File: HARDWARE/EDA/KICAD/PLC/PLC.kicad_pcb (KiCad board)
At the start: 2 copper layers, 200.5 x 200.5 mm, 0 parts

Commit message: Schematic finished
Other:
- outline, holes or cut-outs redrawn
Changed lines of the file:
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@@
   (general
     (thickness 1.6)
-    (drawings 11)
+    (drawings 19)
     (tracks 0)
     (zones 0)
@@
     (uvia_drill 0.1)
   )
+  (gr_circle (center 148 153) (end 146.5 153) (layer Edge.Cuts) (width 0.05))
+  (gr_circle (center 98 103) (end 96.5 103) (layer Edge.Cuts) (width 0.05))
+  (gr_circle (center 148 53) (end 146.5 53) (layer Edge.Cuts) (width 0.05))
+  (gr_circle (center 198 103) (end 196.5 103) (layer Edge.Cuts) (width 0.05))
+  (target plus (at 148 153) (size 5) (width 0.05) (layer Edge.Cuts))
+  (target plus (at 148 53) (size 5) (width 0.05) (layer Edge.Cuts))
+  (target plus (at 198 103) (size 5) (width 0.05) (layer Edge.Cuts))
+  (target plus (at 98 103) (size 5) (width 0.05) (layer Edge.Cuts))
   (gr_circle (center 148 103) (end 243 103) (layer B.SilkS) (width 0.12))
   (gr_circle (center 148 103) (end 243 103) (layer F.SilkS) (width 0.12))

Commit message: pause work
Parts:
- added C1: 250V, Capacitor_THT:CP_Radial_D10.0mm_P5.00mm, F.Cu at (271.8, -24.7)
- added D1: 1N4007, Diode_THT:D_DO-41_SOD81_P10.16mm_Horizontal, F.Cu at (243.7, -0.48)
- added D10: LED 3V, LED_THT:LED_D5.0mm_Clear, F.Cu at (659.8, -7.40)
- added D100: LED 3V, LED_THT:LED_D5.0mm_Clear, F.Cu at (407.5, 15.0)
- added D101: LED 3V, LED_THT:LED_D5.0mm_Clear, F.Cu at (400.0, 22.6)
- added D102: LED 3V, LED_THT:LED_D5.0mm_Clear, F.Cu at (392.5, 30.1)
- added D103: LED 3V, LED_THT:LED_D5.0mm_Clear, F.Cu at (385.0, 37.6)
- added D104: LED 3V, LED_THT:LED_D5.0mm_Clear, F.Cu at (370.0, 52.8)
- added D105: LED 3V, LED_THT:LED_D5.0mm_Clear, F.Cu at (362.5, 60.3)
- added D106: LED 3V, LED_THT:LED_D5.0mm_Clear, F.Cu at (355.0, 67.8)
- added D107: LED 3V, LED_THT:LED_D5.0mm_Clear, F.Cu at (347.5, 75.4)
- added D108: LED 3V, LED_THT:LED_D5.0mm_Clear, F.Cu at (340.0, 83.0)
- added D109: LED 3V, LED_THT:LED_D5.0mm_Clear, F.Cu at (377.5, 52.8)
- added D11: LED 3V, LED_THT:LED_D5.0mm_Clear, F.Cu at (666.6, -7.40)
- added D110: LED 3V, LED_THT:LED_D5.0mm_Clear, F.Cu at (392.5, 37.6)
- added D111: LED 3V, LED_THT:LED_D5.0mm_Clear, F.Cu at (385.0, 45.2)
- added D112: LED 3V, LED_THT:LED_D5.0mm_Clear, F.Cu at (400.0, 60.3)
- added D113: LED 3V, LED_THT:LED_D5.0mm_Clear, F.Cu at (407.5, 22.6)
- added D114: LED 3V, LED_THT:LED_D5.0mm_Clear, F.Cu at (415.0, 15.0)
- added D115: LED 3V, LED_THT:LED_D5.0mm_Clear, F.Cu at (370.0, 60.3)
- added D116: LED 3V, LED_THT:LED_D5.0mm_Clear, F.Cu at (362.5, 67.8)
- added D117: LED 3V, LED_THT:LED_D5.0mm_Clear, F.Cu at (355.0, 75.4)
- added D118: LED 3V, LED_THT:LED_D5.0mm_Clear, F.Cu at (347.5, 83.0)
- added D119: LED 3V, LED_THT:LED_D5.0mm_Clear, F.Cu at (377.5, 60.3)
- added D12: LED 3V, LED_THT:LED_D5.0mm_Clear, F.Cu at (673.4, -7.40)
- added D120: LED 3V, LED_THT:LED_D5.0mm_Clear, F.Cu at (422.5, 15.0)
- added D121: LED 3V, LED_THT:LED_D5.0mm_Clear, F.Cu at (400.0, 15.0)
- added D122: LED 3V, LED_THT:LED_D5.0mm, F.Cu at (370.0, 45.2)
- added D123: LED 3V, LED_THT:LED_D5.0mm, F.Cu at (400.0, 37.6)
- added D124: LED 3V, LED_THT:LED_D5.0mm, F.Cu at (392.5, 45.2)
- added D125: LED 3V, LED_THT:LED_D5.0mm, F.Cu at (385.0, 52.8)
- added D126: LED 3V, LED_THT:LED_D5.0mm, F.Cu at (370.0, 67.8)
- added D127: LED 3V, LED_THT:LED_D5.0mm, F.Cu at (362.5, 75.4)
- added D128: LED 3V, LED_THT:LED_D5.0mm, F.Cu at (355.0, 83.0)
- added D129: LED 3V, LED_THT:LED_D5.0mm, F.Cu at (377.5, 67.8)
- added D13: LED 3V, LED_THT:LED_D5.0mm_Clear, F.Cu at (680.2, -7.40)
- added D130: LED 3V, LED_THT:LED_D5.0mm, F.Cu at (392.5, 52.8)
- added D131: LED 3V, LED_THT:LED_D5.0mm, F.Cu at (415.0, 22.6)
- added D132: LED 3V, LED_THT:LED_D5.0mm, F.Cu at (407.5, 30.1)
- added D133: LED 3V, LED_THT:LED_D5.0mm, F.Cu at (407.5, 37.6)
- added D134: LED 3V, LED_THT:LED_D5.0mm, F.Cu at (415.0, 30.1)
- added D135: LED 3V, LED_THT:LED_D5.0mm, F.Cu at (422.5, 22.6)
- added D136: LED 3V, LED_THT:LED_D5.0mm, F.Cu at (430.0, 15.0)
- added D137: LED 3V, LED_THT:LED_D5.0mm, F.Cu at (370.0, 75.4)
- added D138: LED 3V, LED_THT:LED_D5.0mm, F.Cu at (362.5, 83.0)
- added D139: LED 3V, LED_THT:LED_D5.0mm, F.Cu at (377.5, 75.4)
- added D14: LED 3V, LED_THT:LED_D5.0mm_Clear, F.Cu at (687.0, -7.40)
- added D140: LED 3V, LED_THT:LED_D5.0mm, F.Cu at (430.0, 22.6)
- added D141: LED 3V, LED_THT:LED_D5.0mm, F.Cu at (422.5, 30.1)
- added D142: LED 3V, LED_THT:LED_D5.0mm, F.Cu at (415.0, 37.6)
- added D143: LED 3V, LED_THT:LED_D5.0mm, F.Cu at (407.5, 45.2)
- added D144: LED 3V, LED_THT:LED_D5.0mm, F.Cu at (400.0, 52.8)
- added D145: LED 3V, LED_THT:LED_D5.0mm, F.Cu at (392.5, 60.3)
- added D146: LED 3V, LED_THT:LED_D5.0mm, F.Cu at (385.0, 67.8)
- added D147: LED 3V, LED_THT:LED_D5.0mm, F.Cu at (370.0, 83.0)
- added D148: LED 3V, LED_THT:LED_D5.0mm, F.Cu at (377.5, 83.0)
- added D149: LED 3V, LED_THT:LED_D5.0mm, F.Cu at (392.5, 67.8)
- added D15: LED 3V, LED_THT:LED_D5.0mm_Clear, F.Cu at (693.8, -7.40)
- added D150: LED 3V, LED_THT:LED_D5.0mm, F.Cu at (385.0, 75.4)
- added D151: LED 3V, LED_THT:LED_D5.0mm, F.Cu at (400.0, 30.1)
- added D152: LED 3V, LED_THT:LED_D5.0mm, F.Cu at (407.5, 52.8)
- added D153: LED 3V, LED_THT:LED_D5.0mm, F.Cu at (415.0, 45.2)
- added D154: LED 3V, LED_THT:LED_D5.0mm, F.Cu at (422.5, 37.6)
- added D155: LED 3V, LED_THT:LED_D5.0mm, F.Cu at (430.0, 30.1)
- added D156: LED 3V, LED_THT:LED_D5.0mm, F.Cu at (430.0, 37.6)
- added D157: LED 3V, LED_THT:LED_D5.0mm, F.Cu at (422.5, 45.2)
- added D158: LED 3V, LED_THT:LED_D5.0mm, F.Cu at (415.0, 52.8)
- added D159: LED 3V, LED_THT:LED_D5.0mm, F.Cu at (407.5, 60.3)
- added D16: LED 3V, LED_THT:LED_D5.0mm_Clear, F.Cu at (700.6, -7.40)
- added D160: LED 3V, LED_THT:LED_D5.0mm, F.Cu at (385.0, 60.3)
- added D17: 1N4007, Diode_THT:D_DO-41_SOD81_P10.16mm_Horizontal, F.Cu at (257.6, -4.73)
- added D18: LED 3V, LED_THT:LED_D5.0mm_Clear, F.Cu at (530.6, -7.40)
- added D19: LED 3V, LED_THT:LED_D5.0mm_Clear, F.Cu at (537.4, -7.40)
- added D2: 1N4007, Diode_THT:D_DO-41_SOD81_P10.16mm_Horizontal, F.Cu at (243.7, -4.73)
- added D20: LED 3V, LED_THT:LED_D5.0mm_Clear, F.Cu at (544.2, -7.40)
- added D21: LED 3V, LED_THT:LED_D5.0mm_Clear, F.Cu at (551.0, -7.40)
- added D22: LED 3V, LED_THT:LED_D5.0mm_Clear, F.Cu at (557.8, -7.40)
- added D23: LED 3V, LED_THT:LED_D5.0mm_Clear, F.Cu at (564.6, -7.40)
- added D24: LED 3V, LED_THT:LED_D5.0mm_Clear, F.Cu at (571.4, -7.40)
- added D25: LED 3V, LED_THT:LED_D5.0mm_Clear, F.Cu at (578.2, -7.40)
- added D26: LED 3V, LED_THT:LED_D5.0mm_Clear, F.Cu at (585.0, -7.40)
- added D27: LED 3V, LED_THT:LED_D5.0mm_Clear, F.Cu at (591.8, -7.40)
- added D28: LED 3V, LED_THT:LED_D5.0mm_Clear, F.Cu at (598.6, -7.40)
- added D29: LED 3V, LED_THT:LED_D5.0mm_Clear, F.Cu at (605.4, -7.40)
- added D3: 1N4007, Diode_THT:D_DO-41_SOD81_P10.16mm_Horizontal, F.Cu at (243.7, 3.77)
- added D30: LED 3V, LED_THT:LED_D5.0mm_Clear, F.Cu at (612.2, -7.40)
- added D31: LED 3V, LED_THT:LED_D5.0mm_Clear, F.Cu at (441.4, -7.20)
- added D32: LED 3V, LED_THT:LED_D5.0mm_Clear, F.Cu at (448.2, -7.20)
- added D33: LED 3V, LED_THT:LED_D5.0mm_Clear, F.Cu at (455.0, -7.20)
- added D34: LED 3V, LED_THT:LED_D5.0mm_Clear, F.Cu at (461.8, -7.20)
- added D35: LED 3V, LED_THT:LED_D5.0mm_Clear, F.Cu at (468.6, -7.20)
- added D36: LED 3V, LED_THT:LED_D5.0mm_Clear, F.Cu at (475.4, -7.20)
- added D37: LED 3V, LED_THT:LED_D5.0mm_Clear, F.Cu at (482.2, -7.20)
- added D38: LED 3V, LED_THT:LED_D5.0mm_Clear, F.Cu at (489.0, -7.20)
- added D39: LED 3V, LED_THT:LED_D5.0mm_Clear, F.Cu at (495.8, -7.20)
- added D4: LED 3V, LED_THT:LED_D5.0mm_Clear, F.Cu at (619.0, -7.40)
- added D40: LED 3V, LED_THT:LED_D5.0mm_Clear, F.Cu at (502.6, -7.20)
- added D41: LED 3V, LED_THT:LED_D5.0mm_Clear, F.Cu at (509.4, -7.20)
- added D42: LED 3V, LED_THT:LED_D5.0mm_Clear, F.Cu at (516.4, -7.20)
- added D43: LED 3V, LED_THT:LED_D5.0mm_Clear, F.Cu at (523.8, -7.40)
- added D44: LED 3V, LED_THT:LED_D5.0mm, F.Cu at (349.2, -7.20)
- added D45: LED 3V, LED_THT:LED_D5.0mm, F.Cu at (356.0, -7.20)
- added D46: LED 3V, LED_THT:LED_D5.0mm, F.Cu at (362.8, -7.20)
- added D47: LED 3V, LED_THT:LED_D5.0mm, F.Cu at (369.6, -7.20)
- added D48: LED 3V, LED_THT:LED_D5.0mm, F.Cu at (376.4, -7.20)
- added D49: LED 3V, LED_THT:LED_D5.0mm, F.Cu at (383.4, -7.20)
- added D5: LED 3V, LED_THT:LED_D5.0mm_Clear, F.Cu at (625.8, -7.40)
- added D50: LED 3V, LED_THT:LED_D5.0mm, F.Cu at (390.2, -7.20)
- added D51: LED 3V, LED_THT:LED_D5.0mm, F.Cu at (397.0, -7.20)
- added D52: LED 3V, LED_THT:LED_D5.0mm, F.Cu at (403.8, -7.20)
- added D53: LED 3V, LED_THT:LED_D5.0mm, F.Cu at (410.6, -7.20)
- added D54: LED 3V, LED_THT:LED_D5.0mm, F.Cu at (417.4, -7.20)
- added D55: LED 3V, LED_THT:LED_D5.0mm, F.Cu at (424.2, -7.20)
- added D56: LED 3V, LED_THT:LED_D5.0mm, F.Cu at (431.0, -7.20)
- added D57: LED 3V, LED_THT:LED_D5.0mm, F.Cu at (362.5, 22.6)
- added D58: LED 3V, LED_THT:LED_D5.0mm, F.Cu at (370.0, 15.0)
- added D59: LED 3V, LED_THT:LED_D5.0mm, F.Cu at (377.5, 15.0)
- added D6: LED 3V, LED_THT:LED_D5.0mm_Clear, F.Cu at (632.6, -7.40)
- added D60: LED 3V, LED_THT:LED_D5.0mm, F.Cu at (370.0, 22.6)
- added D61: LED 3V, LED_THT:LED_D5.0mm, F.Cu at (362.5, 30.1)
- added D62: LED 3V, LED_THT:LED_D5.0mm, F.Cu at (355.0, 37.6)
- added D63: LED 3V, LED_THT:LED_D5.0mm, F.Cu at (347.5, 45.2)
- added D64: LED 3V, LED_THT:LED_D5.0mm, F.Cu at (340.0, 52.8)
- added D65: LED 3V, LED_THT:LED_D5.0mm, F.Cu at (332.5, 60.3)
- added D66: LED 3V, LED_THT:LED_D5.0mm, F.Cu at (325.0, 67.8)
- added D67: LED 3V, LED_THT:LED_D5.0mm, F.Cu at (317.5, 75.4)
- added D68: LED 3V, LED_THT:LED_D5.0mm, F.Cu at (310.0, 83.0)
- added D69: LED 3V, LED_THT:LED_D5.0mm, F.Cu at (377.5, 22.6)
- added D7: LED 3V, LED_THT:LED_D5.0mm_Clear, F.Cu at (639.4, -7.40)
- added D70: LED 3V, LED_THT:LED_D5.0mm, F.Cu at (385.0, 15.0)
- added D71: LED 3V, LED_THT:LED_D5.0mm, F.Cu at (370.0, 30.1)
- added D72: LED 3V, LED_THT:LED_D5.0mm, F.Cu at (362.5, 37.6)
- added D73: LED 3V, LED_THT:LED_D5.0mm, F.Cu at (310.0, 60.3)
- added D74: LED 3V, LED_THT:LED_D5.0mm, F.Cu at (347.5, 52.8)
- added D75: LED 3V, LED_THT:LED_D5.0mm, F.Cu at (340.0, 60.3)
- added D76: LED 3V, LED_THT:LED_D5.0mm, F.Cu at (332.5, 67.8)
- added D77: LED 3V, LED_THT:LED_D5.0mm, F.Cu at (325.0, 75.4)
- added D78: LED 3V, LED_THT:LED_D5.0mm, F.Cu at (317.5, 83.0)
- added D79: LED 3V, LED_THT:LED_D5.0mm, F.Cu at (377.5, 30.1)
- added D8: LED 3V, LED_THT:LED_D5.0mm_Clear, F.Cu at (646.2, -7.40)
- added D80: LED 3V, LED_THT:LED_D5.0mm, F.Cu at (392.5, 15.0)
- added D81: LED 3V, LED_THT:LED_D5.0mm, F.Cu at (385.0, 22.6)
- added D82: LED 3V, LED_THT:LED_D5.0mm, F.Cu at (332.5, 52.8)
- added D83: LED 3V, LED_THT:LED_D5.0mm_Clear, F.Cu at (400.0, 45.2)
- added D84: LED 3V, LED_THT:LED_D5.0mm_Clear, F.Cu at (355.0, 52.8)
- added D85: LED 3V, LED_THT:LED_D5.0mm_Clear, F.Cu at (347.5, 60.3)
- added D86: LED 3V, LED_THT:LED_D5.0mm_Clear, F.Cu at (340.0, 67.8)
- added D87: LED 3V, LED_THT:LED_D5.0mm_Clear, F.Cu at (332.5, 75.4)
- added D88: LED 3V, LED_THT:LED_D5.0mm_Clear, F.Cu at (325.0, 83.0)
- added D89: LED 3V, LED_THT:LED_D5.0mm_Clear, F.Cu at (377.5, 37.6)
- added D9: LED 3V, LED_THT:LED_D5.0mm_Clear, F.Cu at (653.0, -7.40)
- added D90: LED 3V, LED_THT:LED_D5.0mm_Clear, F.Cu at (392.5, 22.6)
- added D91: LED 3V, LED_THT:LED_D5.0mm_Clear, F.Cu at (385.0, 30.1)
- added D92: LED 3V, LED_THT:LED_D5.0mm_Clear, F.Cu at (370.0, 37.6)
- added D93: LED 3V, LED_THT:LED_D5.0mm_Clear, F.Cu at (362.5, 45.2)
- added D94: LED 3V, LED_THT:LED_D5.0mm_Clear, F.Cu at (362.5, 52.8)
- added D95: LED 3V, LED_THT:LED_D5.0mm_Clear, F.Cu at (408.8, 81.6)
- added D96: LED 3V, LED_THT:LED_D5.0mm_Clear, F.Cu at (347.5, 67.8)
- added D97: LED 3V, LED_THT:LED_D5.0mm_Clear, F.Cu at (340.0, 75.4)
- added D98: LED 3V, LED_THT:LED_D5.0mm_Clear, F.Cu at (332.5, 83.0)
- added D99: LED 3V, LED_THT:LED_D5.0mm_Clear, F.Cu at (377.5, 45.2)
- added F1: Fuse, Fuse:Fuse_Blade_ATO_directSolder, F.Cu at (249.0, -15.3)
- added F2: Fuse, Fuse:Fuse_Blade_ATO_directSolder, F.Cu at (247.4, -25.8)
- added J1: retified-output, Connector_Phoenix_MC_HighVoltage:PhoenixContact_MC_1,5_2-G-5.08_1x02_P5.08mm_Horizontal, F.Cu at (305.2, -24.4)
- added J2: retified-output, Connector_Phoenix_MC_HighVoltage:PhoenixContact_MC_1,5_2-G-5.08_1x02_P5.08mm_Horizontal, F.Cu at (225.9, -12.0)
- added J3: power, Connector_Phoenix_MC_HighVoltage:PhoenixContact_MC_1,5_3-G-5.08_1x03_P5.08mm_Horizontal, F.Cu at (285.9, -23.6)
- added RV1: Varistor 250V, Varistor:RV_Disc_D12mm_W4mm_P7.5mm, F.Cu at (211.4, -4.59)
- added RV2: Varistor 250V, Varistor:RV_Disc_D12mm_W4mm_P7.5mm, F.Cu at (211.4, -10.2)
- added RV3: Varistor 250V, Varistor:RV_Disc_D12mm_W4mm_P7.5mm, F.Cu at (258.8, -0.55)

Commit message: adjusting PCB
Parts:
- C1: footprint Capacitor_THT:CP_Radial_D10.0mm_P5.00mm -> Capacitor_THT:CP_Radial_D18.0mm_P7.50mm
- J1: moved to B.Cu
- moved D11 652.5 mm to (22.2, 95.5)
- moved D12 645.7 mm to (36.0, 95.5)
- moved D10 641.0 mm to (24.8, 79.5), turned to 180 degrees
- moved D13 639.0 mm to (49.5, 95.5)
- moved D14 631.9 mm to (63.5, 95.5)
- moved D15 624.8 mm to (77.5, 95.5)
- moved D9 620.6 mm to (38.5, 79.5), turned to 180 degrees
- moved D16 616.0 mm to (93.2, 95.5)
- moved D8 600.5 mm to (52.0, 79.5), turned to 180 degrees
- moved D7 579.9 mm to (66.0, 79.5), turned to 180 degrees
- moved D26 567.5 mm to (22.2, 65.8)
- moved D27 560.6 mm to (36.0, 65.8)
- moved D6 559.4 mm to (80.0, 79.5), turned to 180 degrees
- moved D28 554.0 mm to (49.5, 65.8)
- moved D29 546.8 mm to (63.5, 65.8)
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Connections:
- J2 pad 1: Net-(C1-Pad1) -> GNDA
- J2 pad 2: GNDA -> Net-(C1-Pad1)
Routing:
- net Net-(D1-Pad2): track 0.00 -> 49.9 mm
- net GNDA: track 0.00 -> 41.7 mm
- net Earth: track 0.00 -> 40.4 mm
- net Net-(C1-Pad1): track 0.00 -> 38.5 mm
- net Net-(D17-Pad1): track 0.00 -> 32.1 mm
- net Net-(F2-Pad2): track 0.00 -> 8.74 mm
- net Net-(F1-Pad2): track 0.00 -> 8.11 mm
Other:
- board size 200.5 x 200.5 mm -> 271.2 x 200.5 mm

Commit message: finished project
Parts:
- removed J1: retified-output, Connector_Phoenix_MC_HighVoltage:PhoenixContact_MC_1,5_2-G-5.08_1x02_P5.08mm_Horizontal
- moved D128 292.6 mm to (111.2, 22.5), turned to 270 degrees
- moved D148 287.4 mm to (185.5, 70.2), turned to 270 degrees
- moved D129 285.0 mm to (111.2, 34.0), turned to 270 degrees
- moved D127 282.8 mm to (125.0, 25.0), turned to 90 degrees
- moved D130 277.2 mm to (111.2, 46.2), turned to 270 degrees
- moved D149 273.4 mm to (185.5, 82.8), turned to 270 degrees
- moved D131 270.1 mm to (111.2, 58.2), turned to 270 degrees
- moved D126 269.6 mm to (125.0, 36.5), turned to 90 degrees
- moved D140 269.2 mm to (137.5, 22.5), turned to 270 degrees
- moved D155 269.0 mm to (161.5, 46.2), turned to 270 degrees
- moved D154 264.6 mm to (173.5, 60.8), turned to 90 degrees
- moved D132 263.6 mm to (111.2, 70.2), turned to 270 degrees
- moved D150 258.4 mm to (185.5, 96.5), turned to 270 degrees
- moved D153 257.8 mm to (173.5, 72.8), turned to 90 degrees
- moved D141 257.5 mm to (137.5, 34.0), turned to 270 degrees
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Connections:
- D109 pad 1: Net-(D109-Pad1) -> GND
- D134 pad 2: Net-(D109-Pad1) -> Net-(D134-Pad2)
- D56 pad 2: Net-(D31-Pad1) -> GROUP1
- D70 pad 1: GND -> Net-(D134-Pad2)
- D95 pad 2: GROUP1 -> Net-(D31-Pad1)
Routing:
- net Net-(D134-Pad2): track 0.00 -> 268.3 mm
- net GND: track 0.00 -> 148.6 mm, vias 0 -> 1
- net Net-(D31-Pad1): track 0.00 -> 129.2 mm
- net Net-(D22-Pad2): track 0.00 -> 19.3 mm
- net Net-(D115-Pad2): track 0.00 -> 18.7 mm
- net Net-(D154-Pad2): track 0.00 -> 18.7 mm
- net Net-(D76-Pad2): track 0.00 -> 18.6 mm
- net Net-(D37-Pad2): track 0.00 -> 18.2 mm
- net Net-(D61-Pad2): track 0.00 -> 18.1 mm
- net Net-(D139-Pad2): track 0.00 -> 18.1 mm
- net Net-(D100-Pad2): track 0.00 -> 17.9 mm
- net GROUP1: track 0.00 -> 16.9 mm, vias 0 -> 1
- net Net-(D49-Pad2): track 0.00 -> 14.0 mm
- net Net-(D127-Pad2): track 0.00 -> 13.8 mm
- net Net-(D10-Pad1): track 0.00 -> 13.8 mm
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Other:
- outline, holes or cut-outs redrawn

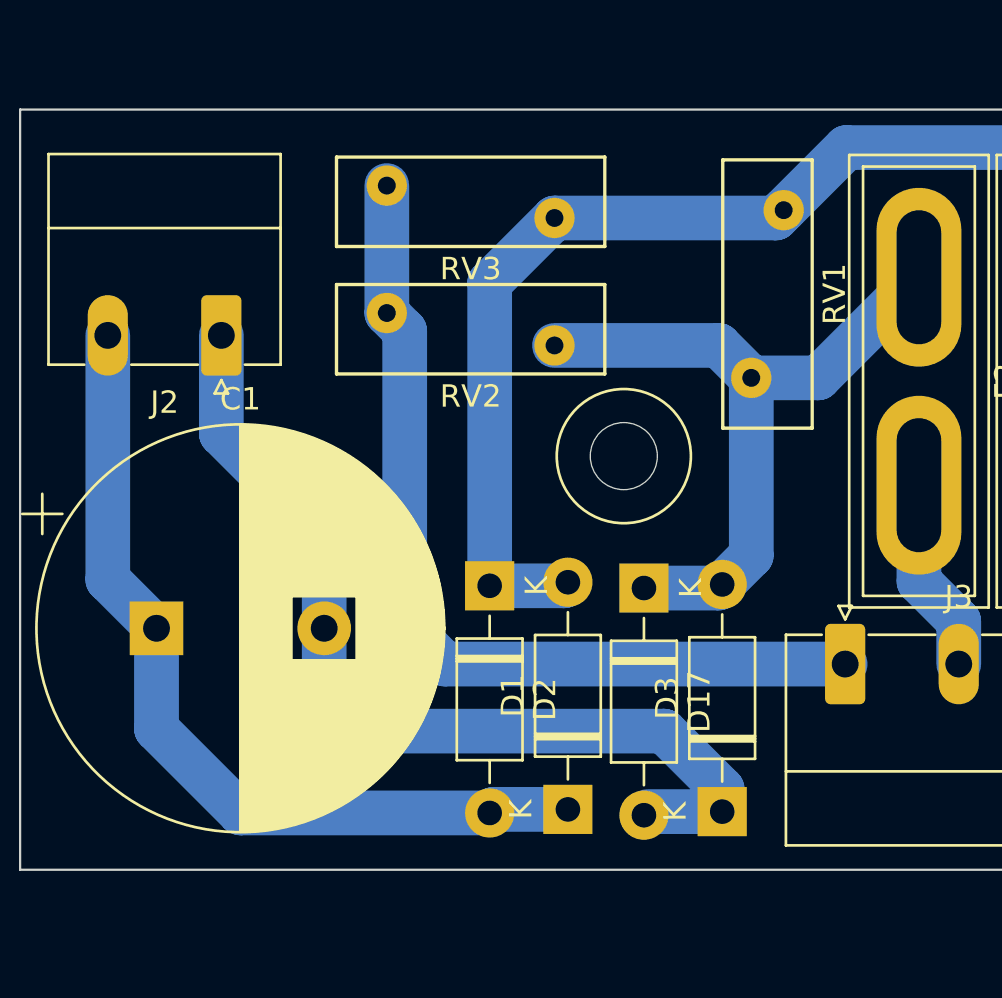
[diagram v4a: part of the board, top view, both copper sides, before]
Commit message: Adjust schematic and PCB
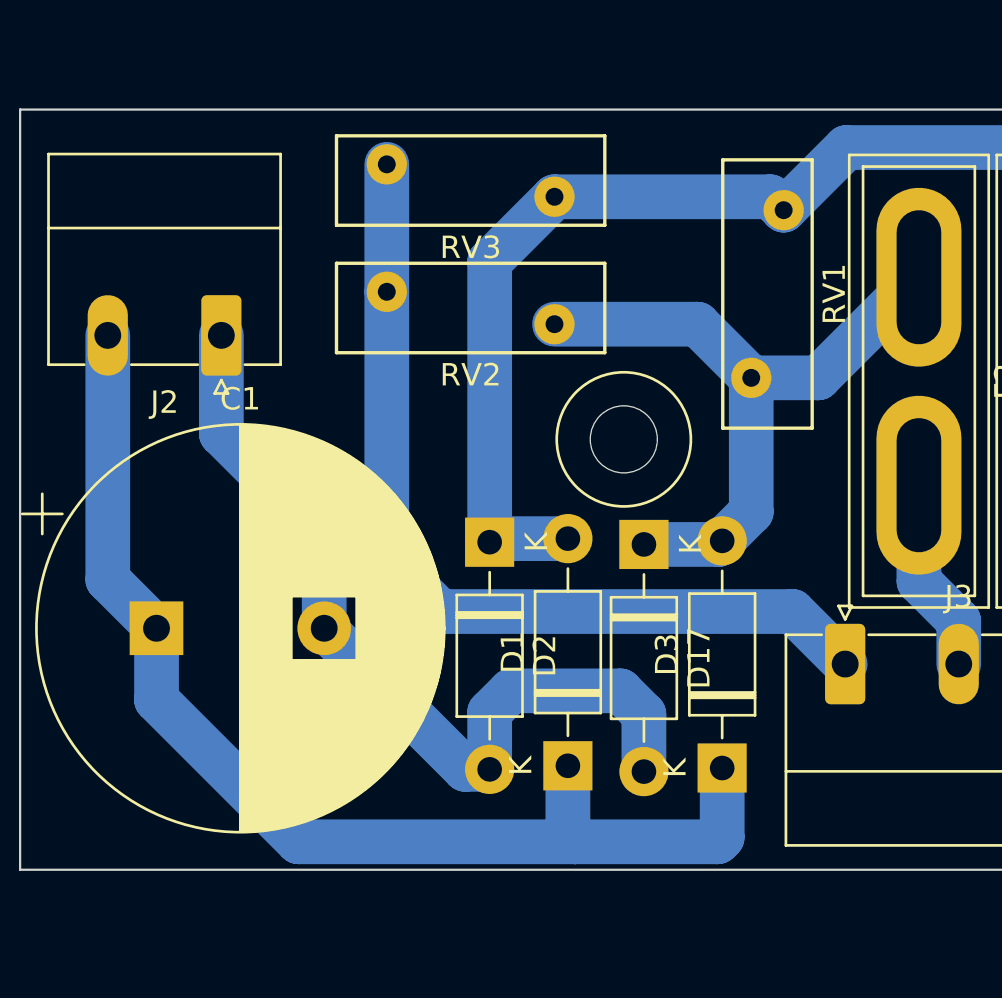
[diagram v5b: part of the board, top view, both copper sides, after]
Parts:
- moved D1 1.95 mm to (248.5, 48.4)
- moved D17 1.95 mm to (251.9, 38.5)
- moved D2 1.95 mm to (245.0, 38.4)
- moved D3 1.95 mm to (255.4, 48.5)
- moved RV2 0.95 mm to (240.4, 27.1)
- moved RV3 0.95 mm to (240.4, 21.4)
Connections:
- D2 pad 2: Net-(C1-Pad1) -> GNDA
- D3 pad 1: GNDA -> Net-(C1-Pad1)
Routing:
- net Net-(C1-Pad1): track 38.5 -> 51.8 mm
- net GNDA: track 41.7 -> 37.9 mm
- net Net-(D17-Pad1): track 32.1 -> 30.6 mm
- net Net-(D1-Pad2): track 49.9 -> 49.0 mm
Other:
- outline, holes or cut-outs redrawn

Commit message: test in pcb
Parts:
- added D10: LED 3V, LED_THT:LED_D5.0mm_Clear, F.Cu at (-263.0, 72.8)
- added D11: LED 3V, LED_THT:LED_D5.0mm_Clear, F.Cu at (-250.8, 72.8)
- added D12: LED 3V, LED_THT:LED_D5.0mm_Clear, F.Cu at (-238.8, 72.8)
- added D13: LED 3V, LED_THT:LED_D5.0mm_Clear, F.Cu at (-226.8, 72.8)
- added D14: LED 3V, LED_THT:LED_D5.0mm_Clear, F.Cu at (-214.8, 72.8)
- added D15: LED 3V, LED_THT:LED_D5.0mm_Clear, F.Cu at (-202.2, 72.8)
- added D16: LED 3V, LED_THT:LED_D5.0mm_Clear, F.Cu at (-188.2, 72.8)
- added D18: LED 3V, LED_THT:LED_D5.0mm_Clear, F.Cu at (-199.8, 34.5)
- added D19: LED 3V, LED_THT:LED_D5.0mm_Clear, F.Cu at (-212.2, 34.5)
- added D20: LED 3V, LED_THT:LED_D5.0mm_Clear, F.Cu at (-224.2, 34.5)
- added D21: LED 3V, LED_THT:LED_D5.0mm_Clear, F.Cu at (-236.2, 34.5)
- added D22: LED 3V, LED_THT:LED_D5.0mm_Clear, F.Cu at (-248.2, 34.5)
- added D23: LED 3V, LED_THT:LED_D5.0mm_Clear, F.Cu at (-263.0, 46.5)
- added D24: LED 3V, LED_THT:LED_D5.0mm_Clear, F.Cu at (-250.8, 46.5)
- added D25: LED 3V, LED_THT:LED_D5.0mm_Clear, F.Cu at (-238.8, 46.5)
- added D26: LED 3V, LED_THT:LED_D5.0mm_Clear, F.Cu at (-226.8, 46.5)
- added D27: LED 3V, LED_THT:LED_D5.0mm_Clear, F.Cu at (-214.8, 46.5)
- added D28: LED 3V, LED_THT:LED_D5.0mm_Clear, F.Cu at (-202.2, 46.5)
- added D29: LED 3V, LED_THT:LED_D5.0mm_Clear, F.Cu at (-188.2, 46.5)
- added D30: LED 3V, LED_THT:LED_D5.0mm_Clear, F.Cu at (-185.8, 59.0)
- added D31: LED 3V, LED_THT:LED_D5.0mm_Clear, F.Cu at (-214.8, -1.25)
- added D32: LED 3V, LED_THT:LED_D5.0mm_Clear, F.Cu at (-202.2, -1.25)
- added D33: LED 3V, LED_THT:LED_D5.0mm_Clear, F.Cu at (-188.2, -1.25)
- added D34: LED 3V, LED_THT:LED_D5.0mm_Clear, F.Cu at (-185.8, 10.2)
- added D35: LED 3V, LED_THT:LED_D5.0mm_Clear, F.Cu at (-199.8, 10.2)
- added D36: LED 3V, LED_THT:LED_D5.0mm_Clear, F.Cu at (-212.2, 10.2)
- added D37: LED 3V, LED_THT:LED_D5.0mm_Clear, F.Cu at (-224.2, 10.2)
- added D38: LED 3V, LED_THT:LED_D5.0mm_Clear, F.Cu at (-238.8, 22.5)
- added D39: LED 3V, LED_THT:LED_D5.0mm_Clear, F.Cu at (-226.8, 22.5)
- added D4: LED 3V, LED_THT:LED_D5.0mm_Clear, F.Cu at (-199.8, 59.0)
- added D40: LED 3V, LED_THT:LED_D5.0mm_Clear, F.Cu at (-214.8, 22.5)
- added D41: LED 3V, LED_THT:LED_D5.0mm_Clear, F.Cu at (-202.2, 22.5)
- added D42: LED 3V, LED_THT:LED_D5.0mm_Clear, F.Cu at (-188.2, 22.5)
- added D43: LED 3V, LED_THT:LED_D5.0mm_Clear, F.Cu at (-185.8, 34.5)
- added D5: LED 3V, LED_THT:LED_D5.0mm_Clear, F.Cu at (-212.2, 59.0)
- added D6: LED 3V, LED_THT:LED_D5.0mm_Clear, F.Cu at (-224.2, 59.0)
- added D7: LED 3V, LED_THT:LED_D5.0mm_Clear, F.Cu at (-236.2, 59.0)
- added D8: LED 3V, LED_THT:LED_D5.0mm_Clear, F.Cu at (-248.2, 59.0)
- added D9: LED 3V, LED_THT:LED_D5.0mm_Clear, F.Cu at (-260.5, 59.0)
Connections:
- D101 pad 2: Net-(D101-Pad2) -> GROUP1
- D102 pad 1: Net-(D101-Pad2) -> GND
- D105 pad 2: Net-(D105-Pad2) -> GROUP1
- D106 pad 1: Net-(D105-Pad2) -> GND
- D109 pad 1: GND -> (no net)
- D111 pad 2: Net-(D111-Pad2) -> GROUP1
- D112 pad 1: Net-(D111-Pad2) -> GND
- D115 pad 2: Net-(D115-Pad2) -> GROUP1
- D116 pad 1: Net-(D115-Pad2) -> GND
- D119 pad 2: Net-(D119-Pad2) -> GROUP1
- D12 pad 2: Net-(D12-Pad2) -> GROUP1
- D120 pad 1: Net-(D119-Pad2) -> GND
- D122 pad 2: Net-(D122-Pad2) -> GROUP1
- D123 pad 1: Net-(D122-Pad2) -> GND
- D126 pad 2: Net-(D126-Pad2) -> GROUP1
- D127 pad 1: Net-(D126-Pad2) -> GND
- D13 pad 1: Net-(D12-Pad2) -> GND
- D130 pad 2: Net-(D130-Pad2) -> GROUP1
- D131 pad 1: Net-(D130-Pad2) -> GND
- D134 pad 2: Net-(D134-Pad2) -> GROUP1
- D136 pad 2: Net-(D136-Pad2) -> GROUP1
- D137 pad 1: Net-(D136-Pad2) -> GND
- D140 pad 2: Net-(D140-Pad2) -> GROUP1
- D141 pad 1: Net-(D140-Pad2) -> GND
- D144 pad 2: Net-(D144-Pad2) -> GROUP1
- D145 pad 1: Net-(D144-Pad2) -> GND
- D148 pad 1: GND -> (no net)
- D150 pad 2: Net-(D150-Pad2) -> GROUP1
- D151 pad 1: Net-(D150-Pad2) -> GND
- D154 pad 2: Net-(D154-Pad2) -> GROUP1
- D155 pad 1: Net-(D154-Pad2) -> GND
- D158 pad 2: Net-(D158-Pad2) -> GROUP1
- D159 pad 1: Net-(D158-Pad2) -> GND
- D19 pad 2: Net-(D19-Pad2) -> GROUP1
- D20 pad 1: Net-(D19-Pad2) -> GND
- D23 pad 2: Net-(D23-Pad2) -> GROUP1
- D24 pad 1: Net-(D23-Pad2) -> GND
- D27 pad 2: Net-(D27-Pad2) -> GROUP1
- D28 pad 1: Net-(D27-Pad2) -> GND
- D31 pad 1: Net-(D31-Pad1) -> (no net)
- D33 pad 2: Net-(D33-Pad2) -> GROUP1
- D34 pad 1: Net-(D33-Pad2) -> GND
- D37 pad 2: Net-(D37-Pad2) -> GROUP1
- D38 pad 1: Net-(D37-Pad2) -> GND
- D4 pad 2: Net-(D4-Pad2) -> GROUP1
- D41 pad 2: Net-(D41-Pad2) -> GROUP1
- D42 pad 1: Net-(D41-Pad2) -> GND
- D44 pad 2: Net-(D44-Pad2) -> GROUP1
- D45 pad 1: Net-(D44-Pad2) -> GND
- D48 pad 2: Net-(D48-Pad2) -> GROUP1
- D49 pad 1: Net-(D48-Pad2) -> GND
- D5 pad 1: Net-(D4-Pad2) -> GND
- D52 pad 2: Net-(D52-Pad2) -> GROUP1
- D53 pad 1: Net-(D52-Pad2) -> GND
- D58 pad 2: Net-(D58-Pad2) -> GROUP1
- D59 pad 1: Net-(D58-Pad2) -> GND
- D62 pad 2: Net-(D62-Pad2) -> GROUP1
- D63 pad 1: Net-(D62-Pad2) -> GND
- D66 pad 2: Net-(D66-Pad2) -> GROUP1
- D67 pad 1: Net-(D66-Pad2) -> GND
- D70 pad 1: Net-(D134-Pad2) -> (no net)
- D72 pad 2: Net-(D72-Pad2) -> GROUP1
- D73 pad 1: Net-(D72-Pad2) -> GND
- D76 pad 2: Net-(D76-Pad2) -> GROUP1
- D77 pad 1: Net-(D76-Pad2) -> GND
- D8 pad 2: Net-(D8-Pad2) -> GROUP1
- D80 pad 2: Net-(D80-Pad2) -> GROUP1
- D81 pad 1: Net-(D80-Pad2) -> GND
- D83 pad 2: Net-(D83-Pad2) -> GROUP1
- D84 pad 1: Net-(D83-Pad2) -> GND
- D87 pad 2: Net-(D87-Pad2) -> GROUP1
- D88 pad 1: Net-(D87-Pad2) -> GND
- D9 pad 1: Net-(D8-Pad2) -> GND
- D91 pad 2: Net-(D91-Pad2) -> GROUP1
- D92 pad 1: Net-(D91-Pad2) -> GND
- D95 pad 2: Net-(D31-Pad1) -> GROUP1
- D97 pad 2: Net-(D97-Pad2) -> GROUP1
- D98 pad 1: Net-(D97-Pad2) -> GND
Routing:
- net GND: track 148.6 -> 1401.9 mm, vias 1 -> 0
- net GROUP1: track 16.9 -> 1267.1 mm, vias 1 -> 0
- net Net-(D134-Pad2): track 268.3 -> 0.00 mm
- net Net-(D31-Pad1): track 129.2 -> 0.00 mm
- net Net-(C1-Pad1): track 51.8 -> 0.00 mm
- net Net-(D1-Pad2): track 49.0 -> 0.00 mm
- net Earth: track 40.1 -> 0.00 mm
- net GNDA: track 37.9 -> 0.00 mm
- net Net-(D17-Pad1): track 30.6 -> 0.00 mm
- net Net-(D115-Pad2): track 18.7 -> 0.00 mm
- net Net-(D154-Pad2): track 18.7 -> 0.00 mm
- net Net-(D76-Pad2): track 18.6 -> 0.00 mm
- net Net-(D37-Pad2): track 18.2 -> 0.00 mm
- net Net-(D150-Pad2): track 12.0 -> 0.00 mm
- net Net-(D72-Pad2): track 12.0 -> 0.00 mm
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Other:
- board size 271.2 x 200.5 mm -> 555.2 x 225.5 mm
